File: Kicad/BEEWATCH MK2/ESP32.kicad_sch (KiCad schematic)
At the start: 41 parts, among them Q1 DMG6968U, SW1 TK-074-4, SW2 TK-074-4, U1 ESP32-S3FH4R2, Y1 40MHz

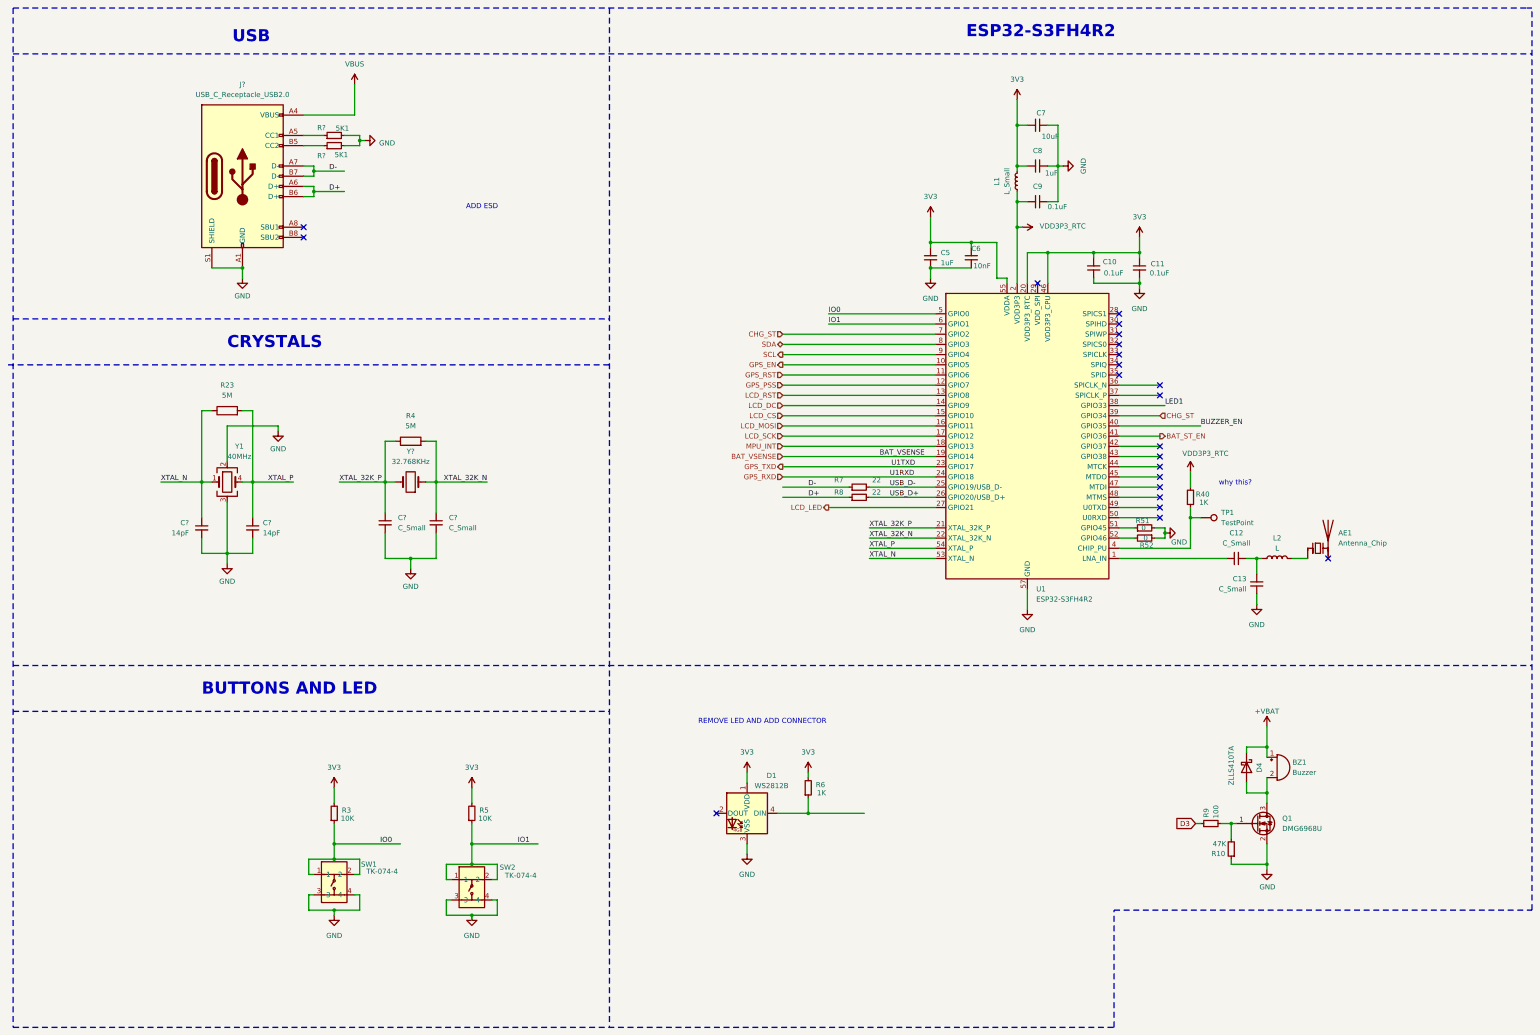
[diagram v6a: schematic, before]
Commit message: Updated to KiCad 9!
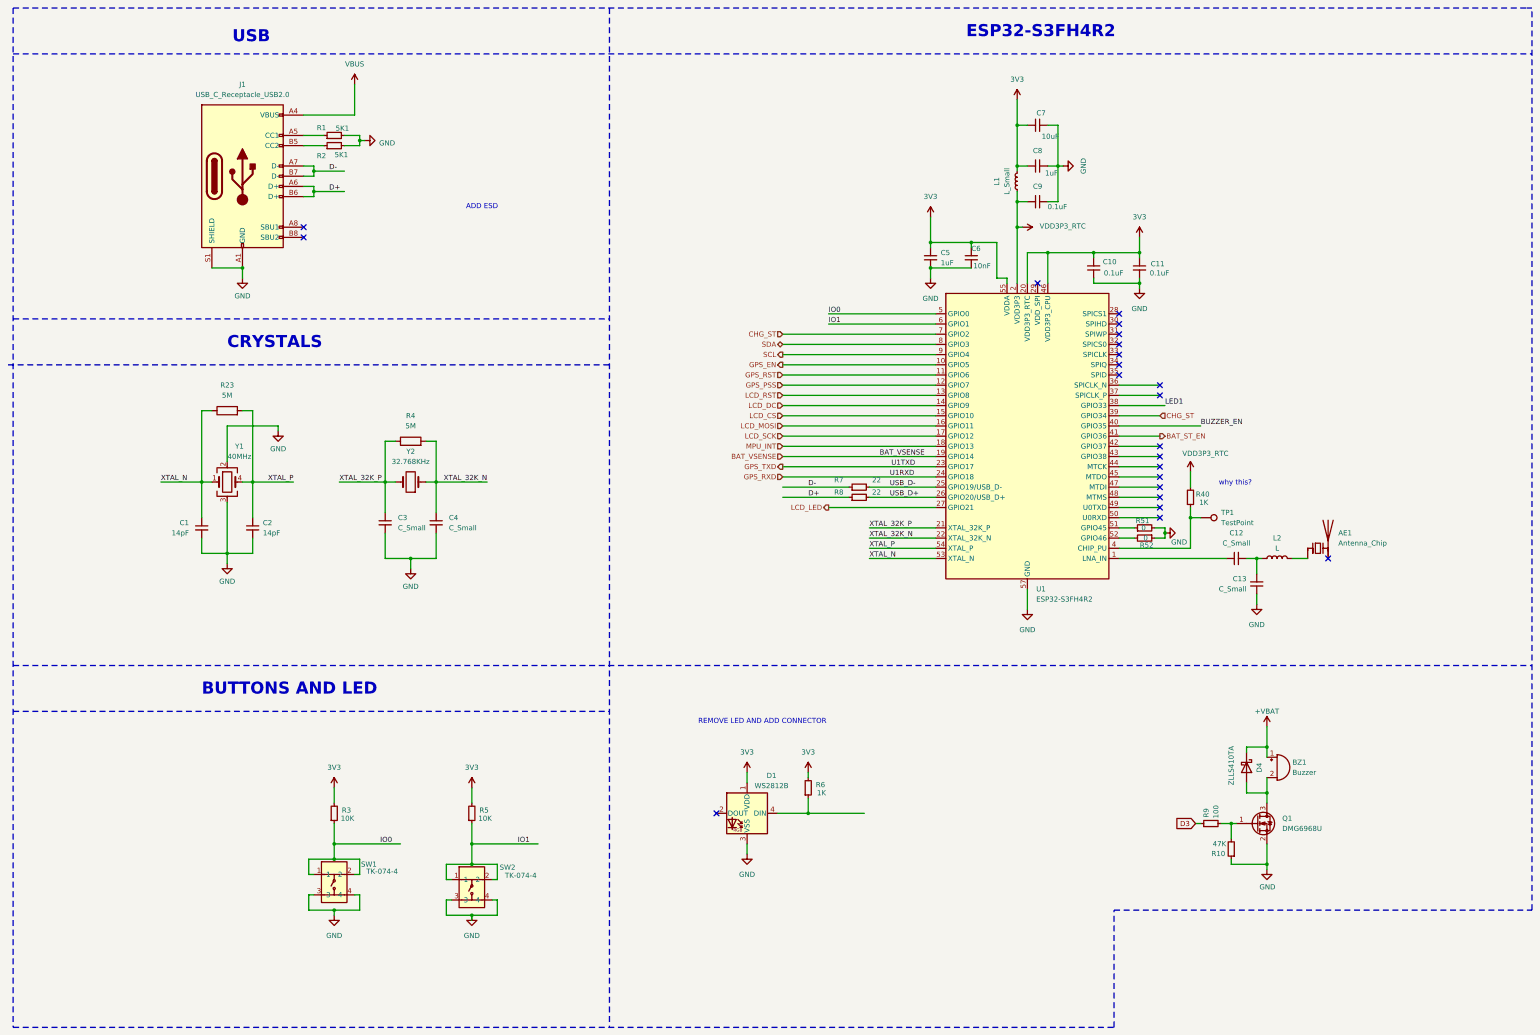
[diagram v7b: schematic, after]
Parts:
- gave numbers to parts that had none: 8
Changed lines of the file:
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@@
 (kicad_sch
-	(version 20231120)
+	(version 20250114)
 	(generator "eeschema")
-	(generator_version "8.0")
+	(generator_version "9.0")
 	(paper "A3")
+	(text "USB"
+		(exclude_from_sim no)
+		(at 74.93 30.48 0)
+		(effects
+			(font
+				(size 3 3)
+				(bold yes)
+			)
+			(justify left bottom)
+		)
+	)
+	(text "CRYSTALS"
+		(exclude_from_sim no)
+		(at 73.66 106.68 0)
+		(effects
+			(font
+				(size 3 3)
+				(bold yes)
+			)
+			(justify left bottom)
+		)
+	)
+	(text "BUTTONS AND LED"
+		(exclude_from_sim no)
+		(at 67.31 193.04 0)
+		(effects
+			(font
+				(size 3 3)
+				(bold yes)
+			)
+			(justify left bottom)
+		)
+	)
+	(text "why this?\n"
+		(exclude_from_sim no)
+		(at 324.866 139.954 0)
+		(effects
+			(font
+				(size 1.27 1.27)
+			)
+		)
+	)
+	(text "ESP32-S3FH4R2"
+		(exclude_from_sim no)
+		(at 257.81 29.21 0)
+		(effects
+			(font
+				(size 3 3)
+				(bold yes)
+			)
+			(justify left bottom)
+		)
+	)
+	(text "REMOVE LED AND ADD CONNECTOR\n"
+		(exclude_from_sim no)
+		(at 207.01 199.39 0)
+		(effects
+			(font
+				(size 1.27 1.27)
+			)
+		)
+	)
+	(text "ADD ESD\n"
+		(exclude_from_sim no)
+		(at 137.16 71.12 0)
+		(effects
+			(font
+				(size 1.27 1.27)
+			)
+		)
+	)
 	(junction
 		(at 67.31 139.7)
@@
 		)
 	)
-	(text "USB"
-		(exclude_from_sim no)
-		(at 74.93 30.48 0)
-		(effects
-			(font
-				(size 3 3)
-				(bold yes)
-			)
-			(justify left bottom)
-		)
-	)
-	(text "CRYSTALS"
-		(exclude_from_sim no)
-		(at 73.66 106.68 0)
-		(effects
-			(font
-				(size 3 3)
-				(bold yes)
-			)
-			(justify left bottom)
-		)
-	)
-	(text "BUTTONS AND LED"
-		(exclude_from_sim no)
-		(at 67.31 193.04 0)
-		(effects
-			(font
-				(size 3 3)
-				(bold yes)
-			)
-			(justify left bottom)
-		)
-	)
-	(text "why this?\n"
-		(exclude_from_sim no)
-		(at 324.866 139.954 0)
-		(effects
-			(font
-				(size 1.27 1.27)
-			)
-		)
-	)
-	(text "ESP32-S3FH4R2"
-		(exclude_from_sim no)
-		(at 257.81 29.21 0)
-		(effects
-			(font
-				(size 3 3)
-				(bold yes)
-			)
-			(justify left bottom)
-		)
-	)
-	(text "REMOVE LED AND ADD CONNECTOR\n"
-		(exclude_from_sim no)
-		(at 207.01 199.39 0)
-		(effects
-			(font
-				(size 1.27 1.27)
-			)
-		)
-	)
-	(text "ADD ESD\n"
-		(exclude_from_sim no)
-		(at 137.16 71.12 0)
-		(effects
-			(font
-				(size 1.27 1.27)
-			)
-		)
-	)
 	(label "IO0"
 		(at 111.76 229.87 0)
@@
 		(dnp no)
 		(fields_autoplaced yes)
-		(property "Reference" "J?"
+		(property "Reference" "J1"
 			(at 77.47 40.64 0)
 			(effects
@@
 		(dnp no)
 		(fields_autoplaced yes)
-		(property "Reference" "#PWR?"
+		(property "Reference" "#PWR07"
 			(at 114.3 54.61 0)
 			(effects
@@
 		(dnp no)
 		(fields_autoplaced yes)
-		(property "Reference" "#PWR?"
+		(property "Reference" "#PWR01"
 			(at 73.66 166.37 0)
 			(effects
@@
 		(on_board yes)
 		(dnp no)
-		(property "Reference" "R?"
+		(property "Reference" "R1"
 			(at 97.155 51.435 90)
 			(effects
@@
 		(on_board yes)
 		(dnp no)
-		(property "Reference" "C?"
+		(property "Reference" "C1"
 			(at 64.135 149.8662 0)
 			(effects
@@
 		(dnp no)
 		(fields_autoplaced yes)
-		(property "Reference" "Y?"
+		(property "Reference" "Y2"
 			(at 119.38 132.08 0)
 			(effects
@@
 		(on_board yes)
 		(dnp no)
-		(property "Reference" "R?"
+		(property "Reference" "R2"
 			(at 97.155 58.42 90)
 			(effects
@@
 		(dnp no)
 		(fields_autoplaced yes)
-		(property "Reference" "C?"
+		(property "Reference" "C4"
 			(at 128.905 148.5962 0)
 			(effects
@@
 		(dnp no)
 		(fields_autoplaced yes)
-		(property "Reference" "#PWR?"
+		(property "Reference" "#PWR08"
 			(at 119.38 167.64 0)
 			(effects
@@
 		(dnp no)
 		(fields_autoplaced yes)
-		(property "Reference" "#PWR?"
+		(property "Reference" "#PWR06"
 			(at 105.41 44.45 0)
 			(effects
@@
 		(dnp no)
 		(fields_autoplaced yes)
-		(property "Reference" "C?"
+		(property "Reference" "C2"
 			(at 82.55 149.8662 0)
 			(effects
@@
 		(dnp no)
 		(fields_autoplaced yes)
-		(property "Reference" "C?"
+		(property "Reference" "C3"
 			(at 116.205 148.5962 0)
 			(effects
@@
 		(dnp no)
 		(fields_autoplaced yes)
-		(property "Reference" "#PWR?"
+		(property "Reference" "#PWR02"
 			(at 77.47 95.25 0)
 			(effects

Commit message: ERC Checking
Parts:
- added R53: 0, Resistor_SMD:R_0402_1005Metric_Pad0.72x0.64mm_HandSolder, symbol Device:R
- Y1: TODO (none) -> ${ERC_ERROR Footprint is sus}
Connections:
- net +VBAT: now also R53.1; no longer BZ1.1 (+), D4.1 (K)
- net LED1: now also D1.4 (DIN), R6.1
- new net: BZ1.1 (+), D4.1 (K), R53.2
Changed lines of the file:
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@@
 	(wire
 		(pts
-			(xy 212.09 130.81) (xy 250.19 130.81)
+			(xy 307.34 198.12) (xy 316.23 198.12)
 		)
 		(stroke
@@
 	(wire
 		(pts
-			(xy 289.56 82.55) (xy 300.99 82.55)
+			(xy 212.09 130.81) (xy 250.19 130.81)
 		)
 		(stroke
@@
 	(wire
 		(pts
-			(xy 273.05 82.55) (xy 273.05 90.17)
+			(xy 289.56 82.55) (xy 300.99 82.55)
 		)
 		(stroke
@@
 	(wire
 		(pts
-			(xy 332.74 200.66) (xy 332.74 205.74)
+			(xy 273.05 82.55) (xy 273.05 90.17)
 		)
 		(stroke
@@
 	(wire
 		(pts
+			(xy 323.85 198.12) (xy 332.74 198.12)
+		)
+		(stroke
+			(width 0)
+			(type default)
+		)
+	)
+	(wire
+		(pts
 			(xy 270.51 69.85) (xy 270.51 76.2)
 		)
@@
 	(wire
 		(pts
+			(xy 332.74 198.12) (xy 332.74 205.74)
+		)
+		(stroke
+			(width 0)
+			(type default)
+		)
+	)
+	(wire
+		(pts
 			(xy 86.36 125.73) (xy 86.36 127)
 		)
@@
 	(wire
 		(pts
+			(xy 307.34 195.58) (xy 307.34 198.12)
+		)
+		(stroke
+			(width 0)
+			(type default)
+		)
+	)
+	(wire
+		(pts
 			(xy 218.44 222.25) (xy 218.44 218.44)
 		)
@@
 		)
 	)
+	(label "LED1"
+		(at 228.6 222.25 0)
+		(effects
+			(font
+				(size 1.27 1.27)
+			)
+			(justify left bottom)
+		)
+	)
 	(label "IO0"
 		(at 111.76 229.87 0)
@@
 	)
 	(symbol
+		(lib_id "Device:R")
+		(at 320.04 198.12 90)
+		(unit 1)
+		(exclude_from_sim no)
+		(in_bom yes)
+		(on_board yes)
+		(dnp no)
+		(fields_autoplaced yes)
+		(property "Reference" "R53"
+			(at 320.04 191.77 90)
+			(effects
+				(font
+					(size 1.27 1.27)
+				)
+			)
+		)
+		(property "Value" "0"
+			(at 320.04 194.31 90)
+			(effects
+				(font
+					(size 1.27 1.27)
+				)
+			)
+		)
+		(property "Footprint" "Resistor_SMD:R_0402_1005Metric_Pad0.72x0.64mm_HandSolder"
+			(at 320.04 199.898 90)
+			(effects
+				(font
+					(size 1.27 1.27)
+				)
+				(hide yes)
+			)
+		)
+		(property "Datasheet" "~"
+			(at 320.04 198.12 0)
+			(effects
+				(font
+					(size 1.27 1.27)
+				)
+				(hide yes)
+			)
+		)
+		(property "Description" "Resistor"
+			(at 320.04 198.12 0)
+			(effects
+				(font
+					(size 1.27 1.27)
+				)
+				(hide yes)
+			)
+		)
+		(pin "1"
+		)
+		(pin "2"
+		)
+		(instances
+			(project "BEEWATCH MK2"
+				(path "/e9c5fb53-480b-4989-8495-a3341ee99514/56d77f8e-c069-456f-a514-fdde13f048cd"
+					(reference "R53")
+					(unit 1)
+				)
+			)
+		)
+	)
+	(symbol
 		(lib_id "Device:R_Small")
 		(at 323.85 231.14 180)
@@
 	(symbol
 		(lib_id "power:+5V")
-		(at 332.74 200.66 0)
+		(at 307.34 195.58 0)
 		(unit 1)
 		(exclude_from_sim no)
@@
 		(fields_autoplaced yes)
 		(property "Reference" "#PWR022"
-			(at 332.74 204.47 0)
+			(at 307.34 199.39 0)
 			(effects
 				(font
@@
 		)
 		(property "Value" "+VBAT"
-			(at 332.74 196.85 0)
+			(at 307.34 191.77 0)
 			(effects
 				(font
@@
 		)
 		(property "Footprint" ""
-			(at 332.74 200.66 0)
+			(at 307.34 195.58 0)
 			(effects
 				(font
@@
 		)
 		(property "Datasheet" ""
-			(at 332.74 200.66 0)
+			(at 307.34 195.58 0)
 			(effects
 				(font
@@
 		)
 		(property "Description" "Power symbol creates a global label with name \"+5V\""
-			(at 332.74 200.66 0)
+			(at 307.34 195.58 0)
 			(effects
 				(font
@@
 		)
 		(instances
-			(project "BEEWATCH MK3"
+			(project "BEEWATCH MK2"
 				(path "/e9c5fb53-480b-4989-8495-a3341ee99514/56d77f8e-c069-456f-a514-fdde13f048cd"
 					(reference "#PWR022")
@@
 			)
 		)
+		(property "TODO" "${ERC_ERROR Footprint is sus}"
+			(at 73.66 139.7 0)
+			(effects
+				(font
+					(size 1.27 1.27)
+				)
+			)
+		)
